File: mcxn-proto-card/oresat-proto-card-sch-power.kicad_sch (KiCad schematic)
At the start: 89 parts, among them Q1 DMP2240UDM, Q2 DMP3050LVT-7, Q7 MOSFET-PCH-SOT23-6, Q8 PMV45EN, Q9 PMV45EN, U10 TPS62111RSA, U11 MIC842LYC5, U12 MIC842LYC5, U2 MAX7310, U3 TS5A21366DCUR, U6 MAX4211

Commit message: Fully routed MCXN947 proto card, still needs final polish.
Big cleanup of the proto card's OPD, bringing it up to modern standards. Also fixed the v2 backplane connector. Added the MCXN937 processor, and breakouts for the unused pins. Switched to the new debug connector, which will be fun. That's it!
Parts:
- removed TP32, TP33, TP41, TP42: Test-Point, oresat-misc:TestPoint-0.75mm-th, symbol oresat-misc:Test-Point-0.75mm-th
- added C10: 100n, oresat-passives:0603-C-NOSILK, symbol Device:C_Small
- added R6: 10K, oresat-passives:0603-C-NOSILK, symbol Device:R_US
- C2: value CL10B104KB8NNNL -> 100n
- Q1: symbol oresat-transistors:DMP2240UDM-7 -> Transistor_FET:Q_Dual_PMOS_G1S2G2D2S1D1
- Q7: value MOSFET-PCH-SOT23-6 -> DMP3050LVT-7
- R1, R2: value RC0603FR-0710KL -> 1k; symbol oresat-passives:R-US -> Device:R_US
- R17: value 10k -> 1k; symbol oresat-passives:R-US -> Device:R_US; DPN P2.7KDBCT-ND -> (none); MFR Panasonic -> (none); MPN ERA-3AEB272V -> (none)
- R24, R3, R60, R61, R62, R63, R65, R66, R67, R68, R69, R70, R71, R72, R73, R74, R75, R77, R78, R79, R80, R81, R82, R83: symbol oresat-passives:R-US -> Device:R_US
- R39, R45, R46, R52, R53, R55, R56, R57, R59: value NP -> 1k; symbol oresat-passives:R-US -> Device:R_US
- R4, R5: value RC0603FR-0710KL -> 10k; symbol oresat-passives:R-US -> Device:R_US
- R40, R54, R58: value NP -> 1k; symbol oresat-passives:R-US -> Device:R_US; now fitted
- R76: value 4.7k -> 1k; symbol oresat-passives:R-US -> Device:R_US; DPN P2.7KDBCT-ND -> (none); MFR Panasonic -> (none); MPN ERA-3AEB272V -> (none)
- U6: value MAX4211 -> MAX4211FETE; symbol oresat-ics:MAX4211FETE -> oresat-ics:MAX4211D/E/F
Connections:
- net GND: now also C10.1, R6.2
- net ON/~{OFF}: now also R76.1; no longer R76.2
- net VPD: now also C10.2
- net at D7.2 (A): now also R76.2; no longer R76.1
- net 4211-IOUT: now reaches R66.2, U6.14 (IOUT)
- net at U6.2 (IN): now also R6.1
- net 3.3V renamed +3.3V
- net BOOT0 renamed ~{BOOT}
- net PA2/USART2_TX renamed ISP-UART_TXD
- net PA3/USART2_RX renamed ISP-UART_RXD
- net PEN-SCL-FILT renamed OPD-SCL-INT
- net PEN-SDA-FILT renamed OPD-SDA-INT
- net POUT: no longer names the net of TP2.1, U6.13 (POUT)
- no-connect marks 0 -> 1
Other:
- note added: "250 ms inhibit on power up"
- note added: "@ 1.5 A max"
- note added: "Address selection for Card: 0x10"
- note added: "FIXME"
- note added: "Feedback settings trips at 295m mA"
- note added: "ON/~{OFF} signal powers MAX4211 + TS5A Saves quiescent OPD power draw"
- note added: "OreSat Power Domain (OPD) Power Supply from C3 (3.3V)"
- note added: "PFM Power saving mode enabled"
- note removed: "#caps here just for smoothing?"
- note removed: "(3.3V)"
- note removed: "Address selection for Card (See MAX7310 datasheet)"
- note removed: "Datasheet (pg 24) says this is for overpowered circuit breaker -otherwise pullup COUT1 and COUT2 high Also add manual reset here if needed"
- note removed: "Design notes on table 3 of data sheet"
- note removed: "IS 10k OK? Testing Required Should be like every other 10k"
- note removed: "Note: Address 0b0111110x is reserved on all oresat cards"
- note removed: "OreSat Power Domain (OPD) Power Supply (3.3V)"
- company: (none) -> Portland State Aerospace Society
- title: OreSat M0 Proto Card: Power -> OreSat MCXN Proto Card
- moved on the sheet: C1, C11, C16, C17, C2, C22, C23, C3, C4, C5, C8, C9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

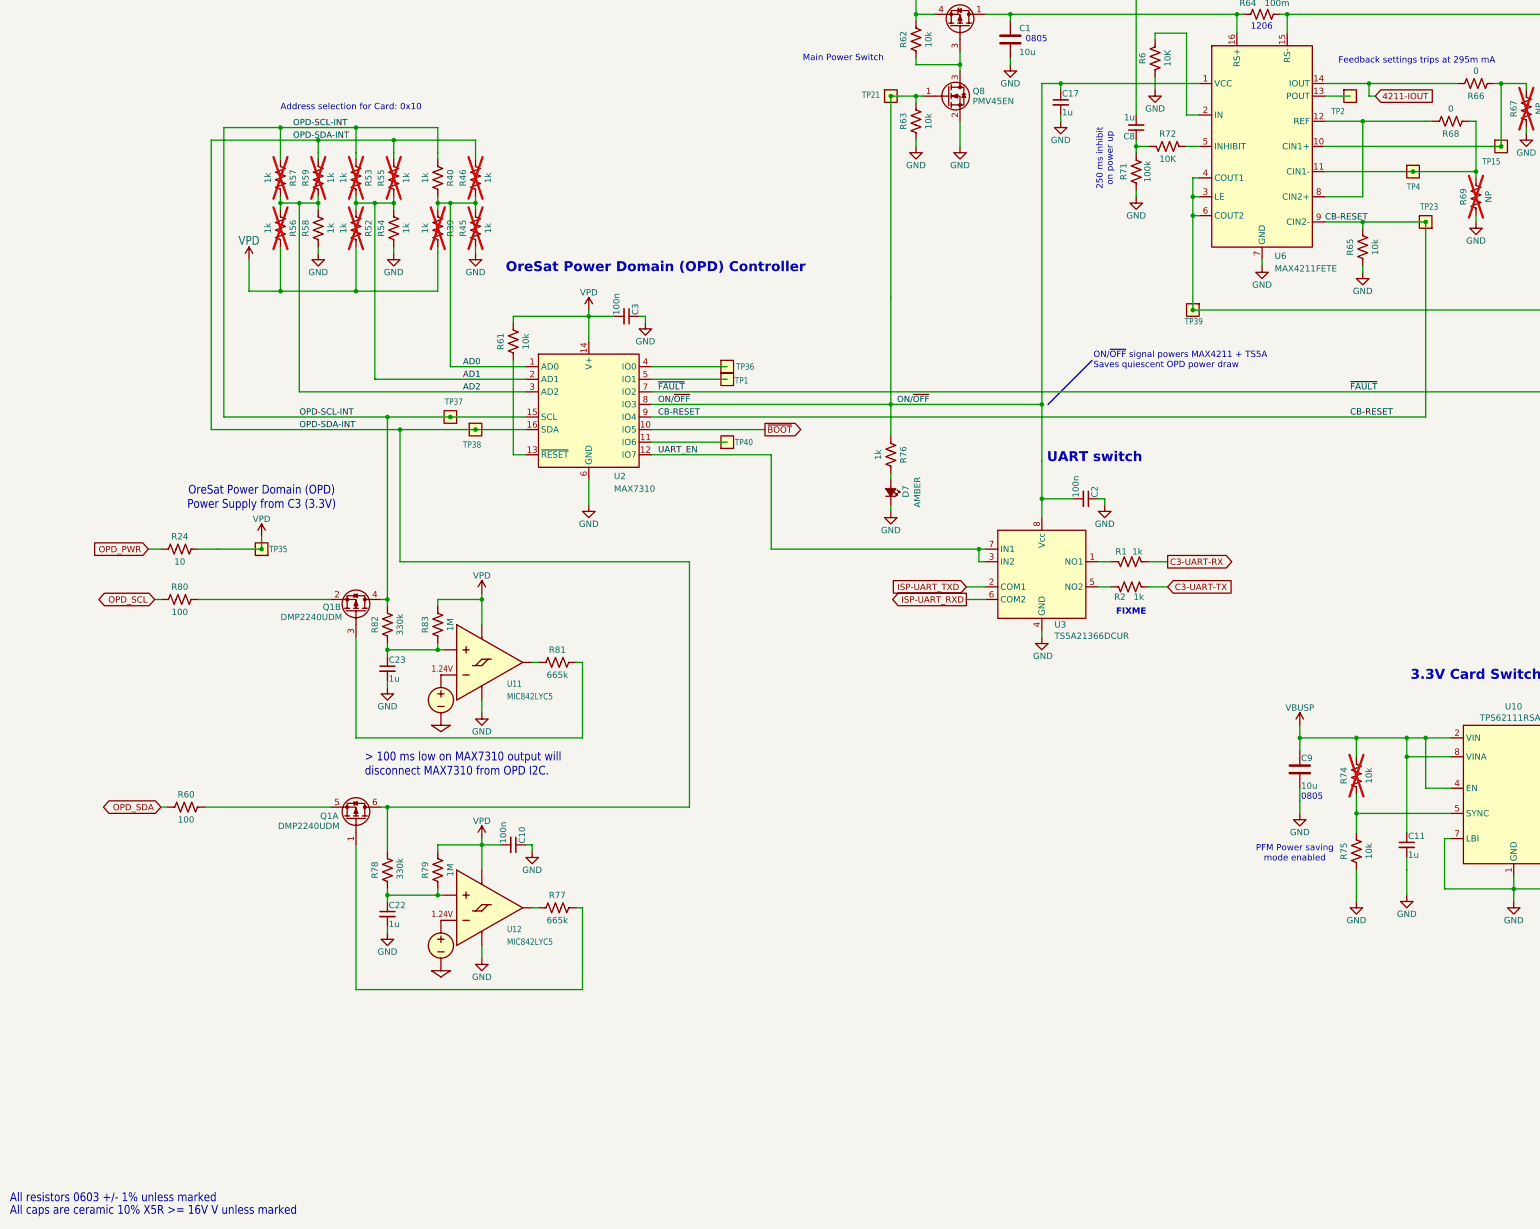
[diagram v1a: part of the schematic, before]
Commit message: Final MCXN protocard cleanup
Made schematic fancy with hierarchical pins, cleaned up schematics a bit, and fixed silk screen a ton. Ready for fab.
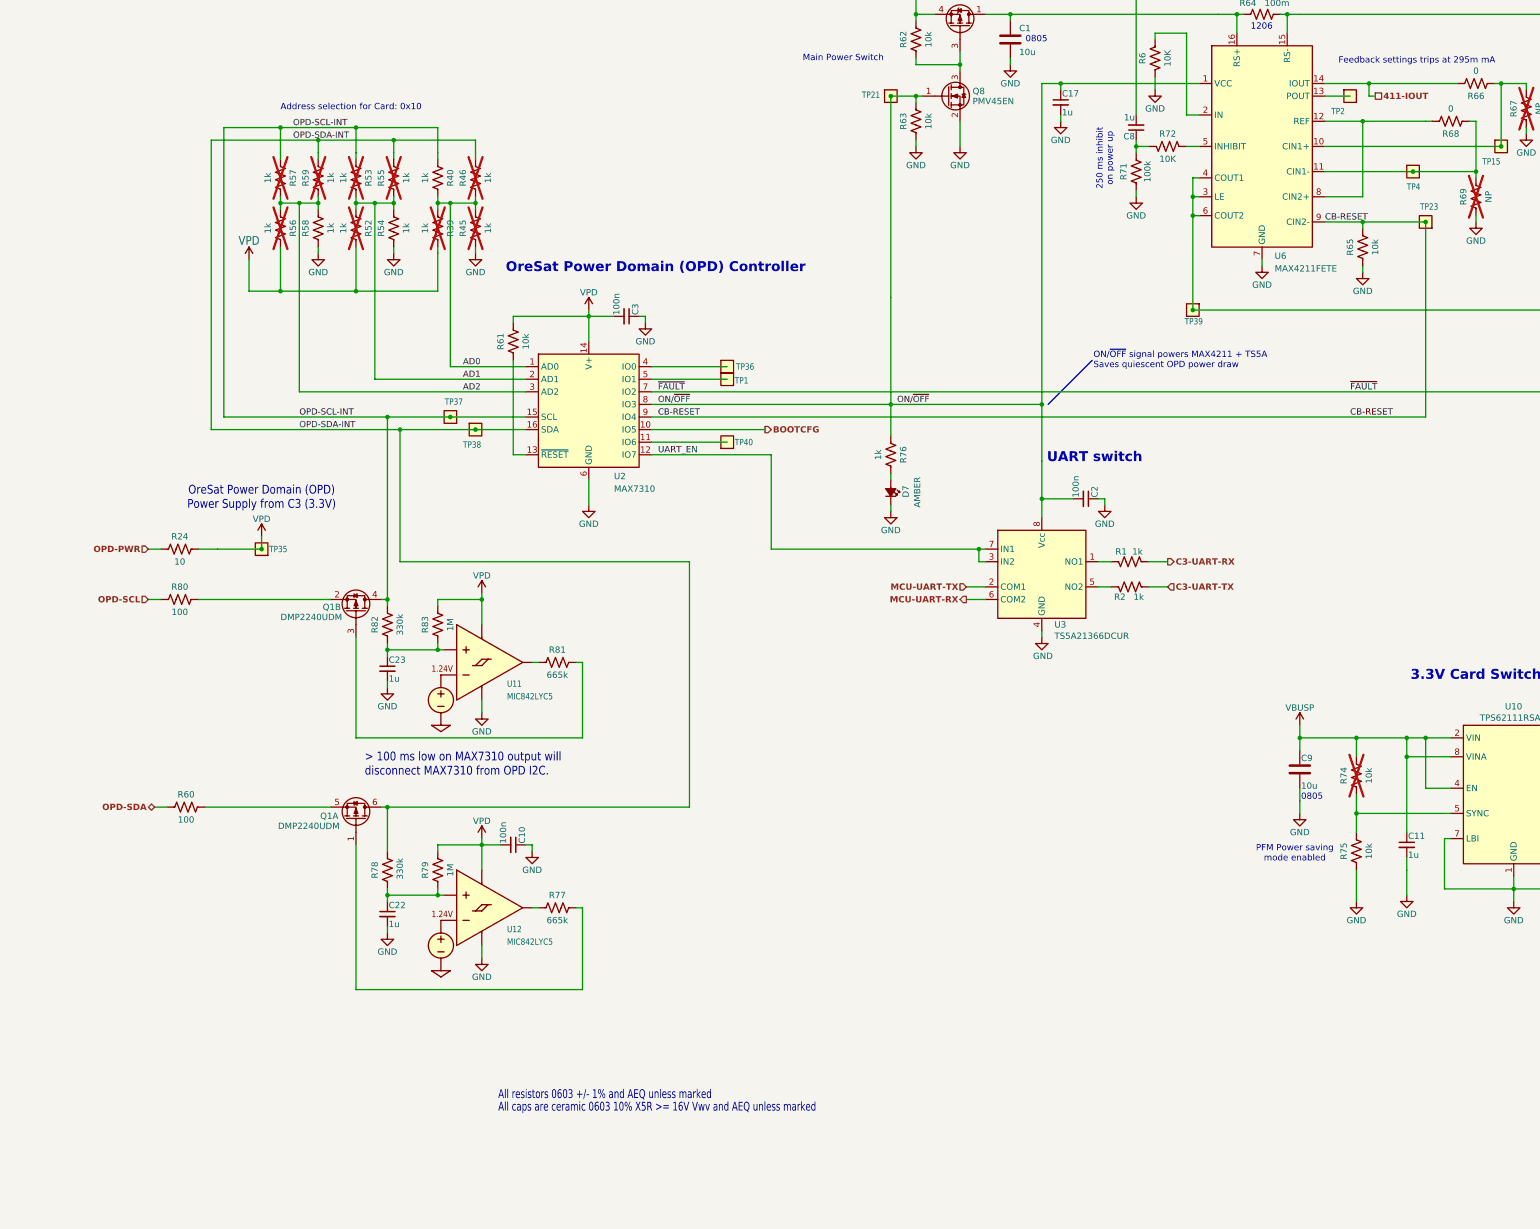
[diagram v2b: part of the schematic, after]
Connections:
- net 4211-IOUT renamed 411-IOUT
- net ISP-UART_RXD renamed MCU-UART-RX
- net ISP-UART_TXD renamed MCU-UART-TX
- net OPD_PWR renamed OPD-PWR
- net OPD_SCL renamed OPD-SCL
- net OPD_SDA renamed OPD-SDA
- net ~{BOOT} renamed BOOTCFG
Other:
- note added: "All caps are ceramic 0603 10% X5R >= 16V Vwv and AEQ unless marked"
- note added: "All resistors 0603 +/- 1% and AEQ unless marked"
- note removed: "All caps are ceramic 10% X5R >= 16V V unless marked"
- note removed: "All resistors 0603 +/- 1% unless marked"
- note removed: "FIXME"
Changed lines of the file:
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@@
 	(title_block
 		(title "OreSat MCXN Proto Card")
-		(date "2025-11-13")
+		(date "2025-12-28")
 		(rev "6.0")
 		(company "Portland State Aerospace Society")
@@
 		)
 	)
-	(text "All caps are ceramic 10% X5R >= 16V V unless marked"
-		(exclude_from_sim no)
-		(at 15.24 287.02 0)
-		(effects
-			(font
-				(size 1.778 1.5113)
-			)
-			(justify left bottom)
-		)
-	)
 	(text "3.3V Card Switching Supply"
 		(exclude_from_sim no)
@@
 		)
 	)
-	(text "All resistors 0603 +/- 1% unless marked"
-		(exclude_from_sim no)
-		(at 15.24 284.48 0)
-		(effects
-			(font
-				(size 1.778 1.5113)
-			)
-			(justify left bottom)
-		)
-	)
 	(text "OreSat Power Domain (OPD)\nPower Supply from C3 (3.3V)"
 		(exclude_from_sim no)
@@
 		)
 	)
+	(text "All resistors 0603 +/- 1% and AEQ unless marked"
+		(exclude_from_sim no)
+		(at 113.792 263.652 0)
+		(effects
+			(font
+				(size 1.778 1.27)
+			)
+			(justify left bottom)
+		)
+	)
 	(text "0805"
 		(exclude_from_sim no)
@@
 		)
 	)
+	(text "All caps are ceramic 0603 10% X5R >= 16V Vwv and AEQ unless marked"
+		(exclude_from_sim no)
+		(at 113.792 266.192 0)
+		(effects
+			(font
+				(size 1.778 1.27)
+			)
+			(justify left bottom)
+		)
+	)
 	(text "250 ms inhibit\non power up"
 		(exclude_from_sim no)
@@
 		)
 	)
-	(text "FIXME"
-		(exclude_from_sim no)
-		(at 241.554 165.1 0)
-		(effects
-			(font
-				(size 1.27 1.27)
-				(thickness 0.254)
-				(bold yes)
-				(color 255 0 0 1)
-			)
-		)
-	)
 	(text "Address selection for Card: 0x10"
 		(exclude_from_sim no)
@@
 	(wire
 		(pts
+			(xy 44.45 204.47) (xy 46.99 204.47)
+		)
+		(stroke
+			(width 0)
+			(type default)
+		)
+	)
+	(wire
+		(pts
 			(xy 344.17 57.15) (xy 344.17 62.23)
 		)
@@
 	(wire
 		(pts
-			(xy 45.72 204.47) (xy 46.99 204.47)
-		)
-		(stroke
-			(width 0)
-			(type default)
-		)
-	)
-	(wire
-		(pts
 			(xy 198.12 60.96) (xy 198.12 62.23)
 		)
@@
 	(wire
 		(pts
-			(xy 45.72 162.56) (xy 44.45 162.56)
+			(xy 45.72 162.56) (xy 43.18 162.56)
 		)
 		(stroke
@@
 		)
 	)
-	(global_label "OPD_SCL"
-		(shape bidirectional)
-		(at 44.45 162.56 180)
-		(fields_autoplaced yes)
+	(hierarchical_label "C3-UART-TX"
+		(shape input)
+		(at 248.92 160.02 0)
 		(effects
 			(font
 				(size 1.27 1.27)
+				(thickness 0.254)
+				(bold yes)
 			)
-			(justify right)
-		)
-		(property "Intersheetrefs" "${INTERSHEET_REFS}"
-			(at 32.0078 162.56 0)
-			(effects
-				(font
-					(size 1.27 1.27)
-				)
-				(justify right)
-			)
+			(justify left)
 		)
 	)
-	(global_label "OPD_SDA"
-		(shape bidirectional)
-		(at 45.72 204.47 180)
-		(fields_autoplaced yes)
+	(hierarchical_label "OPD-SCL"
+		(shape input)
+		(at 43.18 162.56 180)
 		(effects
 			(font
 				(size 1.27 1.27)
+				(thickness 0.254)
+				(bold yes)
 			)
 			(justify right)
 		)
-		(property "Intersheetrefs" "${INTERSHEET_REFS}"
-			(at 33.2173 204.47 0)
-			(effects
-				(font
-					(size 1.27 1.27)
-				)
-				(justify right)
-			)
-		)
 	)
-	(global_label "4211-IOUT"
-		(shape input)
-		(at 290.83 60.96 0)
-		(fields_autoplaced yes)
+	(hierarchical_label "C3-UART-RX"
+		(shape output)
+		(at 248.92 154.94 0)
 		(effects
 			(font
 				(size 1.27 1.27)
+				(thickness 0.254)
+				(bold yes)
 			)
 			(justify left)
 		)
-		(property "Intersheetrefs" "${INTERSHEET_REFS}"
-			(at 304.459 60.96 0)
-			(effects
-				(font
-					(size 1.27 1.27)
-				)
-				(justify left)
-			)
-		)
 	)
-	(global_label "ISP-UART_TXD"
-		(shape input)
-		(at 208.28 160.02 180)
-		(fields_autoplaced yes)
+	(hierarchical_label "411-IOUT"
+		(shape passive)
+		(at 290.83 60.96 0)
 		(effects
 			(font
 				(size 1.27 1.27)
+				(thickness 0.254)
+				(bold yes)
 			)
-			(justify right)
-		)
-		(property "Intersheetrefs" "${INTERSHEET_REFS}"
-			(at 191.5667 160.02 0)
-			(effects
-				(font
-					(size 1.27 1.27)
-				)
-				(justify right)
-			)
+			(justify left)
 		)
 	)
-	(global_label "OPD_PWR"
-		(shape input)
-		(at 43.18 152.4 180)
-		(fields_autoplaced yes)
+	(hierarchical_label "BOOTCFG"
+		(shape output)
+		(at 167.64 128.27 0)
 		(effects
 			(font
 				(size 1.27 1.27)
+				(thickness 0.254)
+				(bold yes)
 			)
-			(justify right)
-		)
-		(property "Intersheetrefs" "${INTERSHEET_REFS}"
-			(at 31.3653 152.4 0)
-			(effects
-				(font
-					(size 1.27 1.27)
-				)
-				(justify right)
-			)
+			(justify left)
 		)
 	)
-	(global_label "ISP-UART_RXD"
+	(hierarchical_label "MCU-UART-RX"
 		(shape output)
 		(at 208.28 162.56 180)
-		(fields_autoplaced yes)
 		(effects
 			(font
 				(size 1.27 1.27)
+				(thickness 0.254)
+				(bold yes)
 			)
 			(justify right)
 		)
-		(property "Intersheetrefs" "${INTERSHEET_REFS}"
-			(at 191.2643 162.56 0)
-			(effects
-				(font
-					(size 1.27 1.27)
-				)
-				(justify right)
-			)
-		)
 	)
-	(global_label "C3-UART-RX"
-		(shape output)
-		(at 248.92 154.94 0)
-		(fields_autoplaced yes)
+	(hierarchical_label "OPD-PWR"
+		(shape input)
+		(at 43.18 152.4 180)
 		(effects
 			(font
 				(size 1.27 1.27)
+				(thickness 0.254)
+				(bold yes)
 			)
-			(justify left)
-		)
-		(property "Intersheetrefs" "${INTERSHEET_REFS}"
-			(at 264.5863 154.94 0)
-			(effects
-				(font
-					(size 1.27 1.27)
-				)
-				(justify left)
-			)
+			(justify right)
 		)
 	)
-	(global_label "C3-UART-TX"
+	(hierarchical_label "MCU-UART-TX"
 		(shape input)
-		(at 248.92 160.02 0)
-		(fields_autoplaced yes)
+		(at 208.28 160.02 180)
 		(effects
 			(font
 				(size 1.27 1.27)
+				(thickness 0.254)
+				(bold yes)
 			)
-			(justify left)
-		)
-		(property "Intersheetrefs" "${INTERSHEET_REFS}"
-			(at 264.2839 160.02 0)
-			(effects
-				(font
-					(size 1.27 1.27)
-				)
-				(justify left)
-			)
+			(justify right)
 		)
 	)
-	(global_label "~{BOOT}"
-		(shape output)
-		(at 167.64 128.27 0)
-		(fields_autoplaced yes)
+	(hierarchical_label "OPD-SDA"
+		(shape bidirectional)
+		(at 44.45 204.47 180)
 		(effects
 			(font
 				(size 1.27 1.27)
+				(thickness 0.254)
+				(bold yes)
 			)
-			(justify left)
-		)
-		(property "Intersheetrefs" "${INTERSHEET_REFS}"
-			(at 175.5238 128.27 0)
-			(effects
-				(font
-					(size 1.27 1.27)
-				)
-				(justify left)
-			)
+			(justify right)
 		)
 	)
